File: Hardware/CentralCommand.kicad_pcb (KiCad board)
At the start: 4 copper layers, 65 parts, among them IC101 STM32F030C8, IC201 FT232RQ, P101 I2C, P102 GPIO1, P103 GPIO1, P104 USART, P105 SPI, P106 ADC, P201 USB_OTG, P202 POWER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

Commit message: layout almost done
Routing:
- net GND: track 89.1 -> 101.6 mm, vias 15 -> 21
- net /PWR: track 29.6 -> 41.4 mm, vias 6 -> 9
- net Net-(C107-Pad1): track 0.00 -> 7.28 mm, vias 0 -> 1

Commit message: relocated footprint labels
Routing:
- net /NRST: track 90.5 -> 92.0 mm
- net GND: track 101.6 -> 103.0 mm, vias 21 -> 22
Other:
- rule pad_to_mask_clearance: 0.2 -> 0.0635

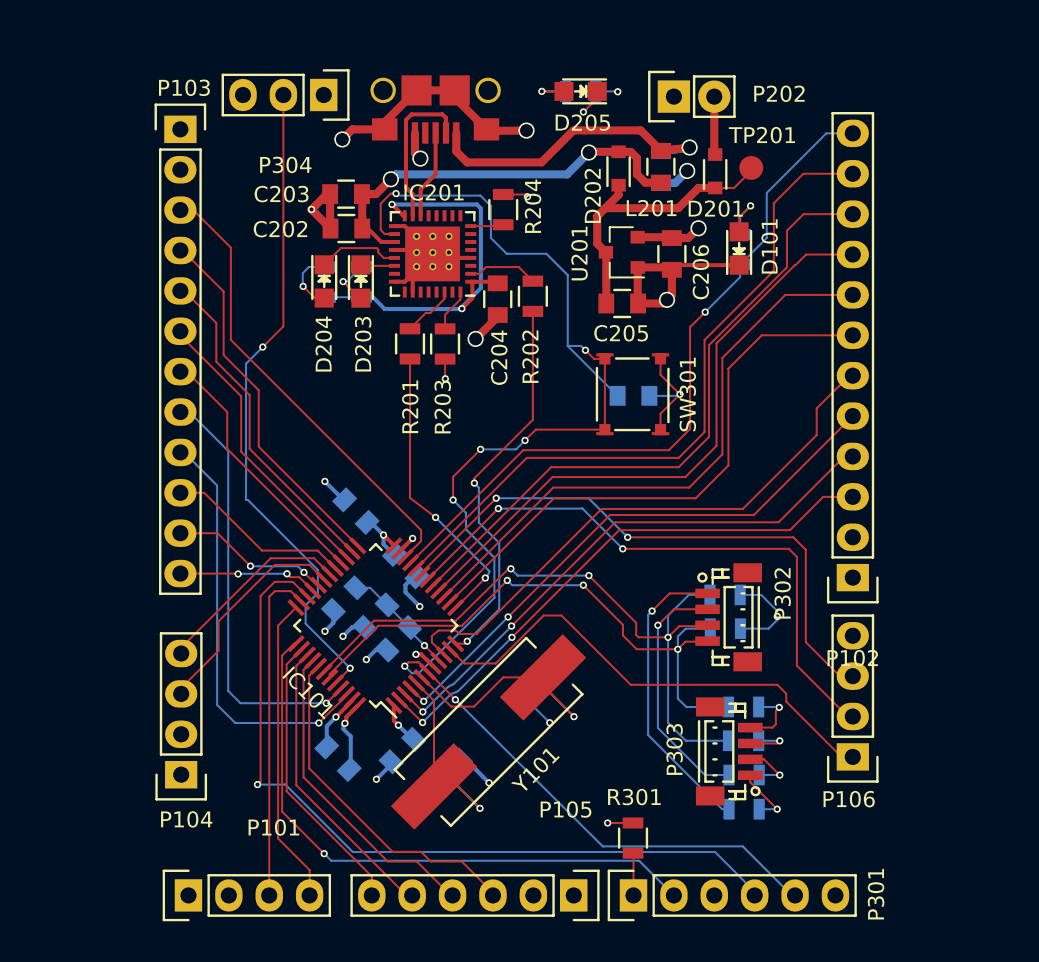
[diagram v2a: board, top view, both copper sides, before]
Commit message: labeled headers
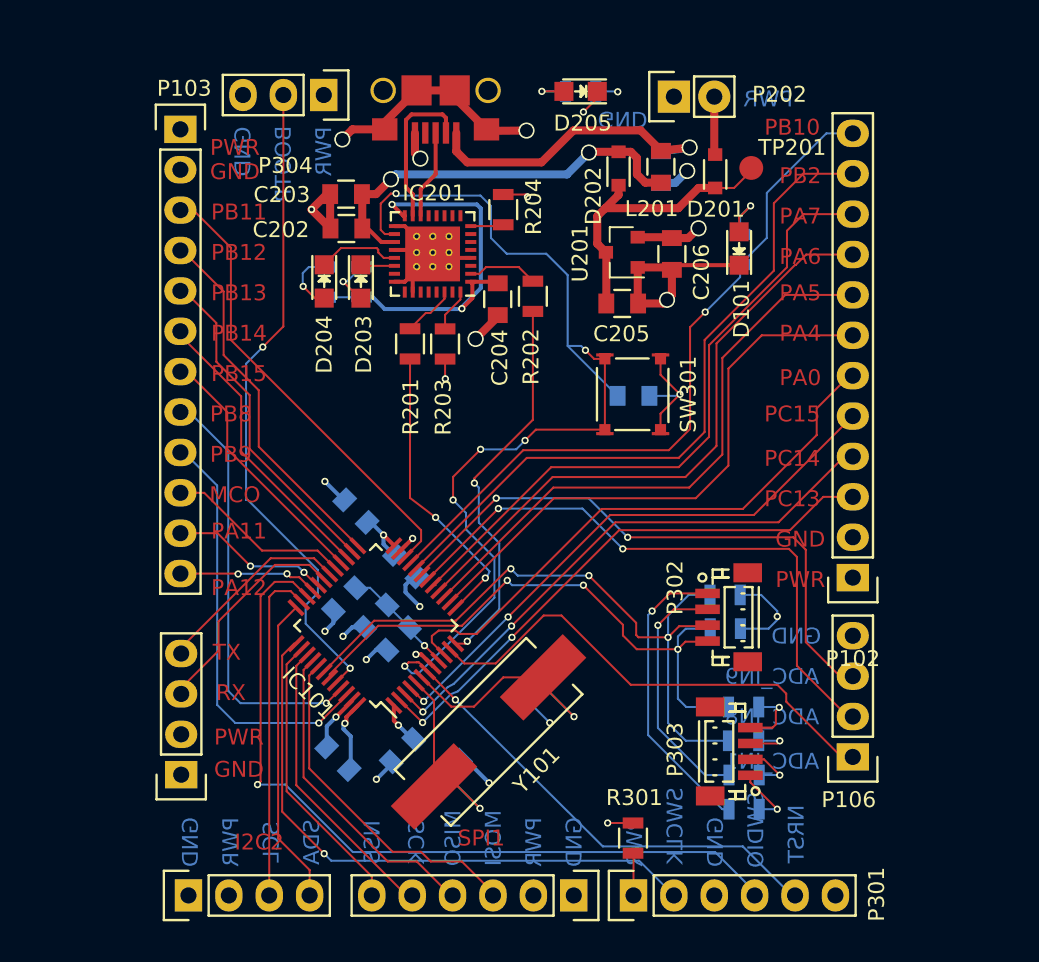
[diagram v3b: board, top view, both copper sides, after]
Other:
- board text added: "ADC_IN1"
- board text added: "ADC_IN8"
- board text added: "ADC_IN9"
- board text added: "BOOTP"
- board text added: "GND"
- board text added: "I2C2"
- board text added: "MCO"
- board text added: "MISO"
- board text added: "MOSI"
- board text added: "NRST"
- board text added: "NSS"
- board text added: "PA0"
- board text added: "PA11"
- board text added: "PA12"
- board text added: "PA4"
- board text added: "PA5"
- board text added: "PA6"
- board text added: "PA7"
- board text added: "PB10"
- board text added: "PB11"
- board text added: "PB12"
- board text added: "PB13"
- board text added: "PB14"
- board text added: "PB15"
- board text added: "PB2"
- board text added: "PB8"
- board text added: "PB9"
- board text added: "PC13"
- board text added: "PC14"
- board text added: "PC15"
- board text added: "PWR"
- board text added: "RX"
- board text added: "SCK"
- board text added: "SCL"
- board text added: "SDA"
- board text added: "SPI1"
- board text added: "SWCLK"
- board text added: "SWDIO"
- board text added: "TX"
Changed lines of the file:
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@@
     (links 170)
     (no_connects 0)
-    (area 102.583 63.83244 154.41038 122.4394)
+    (area 106.174999 62.9536 154.41038 122.4394)
     (thickness 1.6)
-    (drawings 0)
+    (drawings 54)
     (tracks 712)
     (zones 0)
@@
     (solder_mask_min_width 0.0635)
     (aux_axis_origin 0 0)
-    (visible_elements FFFEBD5F)
+    (visible_elements FFFEFF7F)
     (pcbplotparams
       (layerselection 0x00030_80000001)
@@
     (descr "Through hole pin header")
     (tags "pin header")
-    (fp_text reference P101 (at 4.23672 5.36956 180) (layer F.SilkS)
+    (fp_text reference P101 (at 4.23672 5.36956 180) (layer F.SilkS) hide
       (effects (font (size 1 1) (thickness 0.15)))
     )
@@
     (descr "Through hole pin header")
     (tags "pin header")
-    (fp_text reference P104 (at -0.32004 -2.84988 180) (layer F.SilkS)
+    (fp_text reference P104 (at -0.32004 -2.84988 180) (layer F.SilkS) hide
       (effects (font (size 1 1) (thickness 0.15)))
     )
@@
     (descr "Through hole pin header")
     (tags "pin header")
-    (fp_text reference P105 (at -5.36956 0.49276 360) (layer F.SilkS)
+    (fp_text reference P105 (at -5.36956 0.49276 360) (layer F.SilkS) hide
       (effects (font (size 1 1) (thickness 0.15)))
     )
@@
     (tags "connector jst sh")
     (attr smd)
-    (fp_text reference P302 (at -1.5 -3.5 270) (layer F.SilkS)
+    (fp_text reference P302 (at -1.85928 3.302 270) (layer F.SilkS)
       (effects (font (size 1 1) (thickness 0.15)))
     )
@@
     (tags "Mesurement Point Round SMD Pad 1.5mm")
     (attr virtual)
-    (fp_text reference TP201 (at 0.7366 -2.02692) (layer F.SilkS)
+    (fp_text reference TP201 (at 2.57556 -1.28524) (layer F.SilkS)
       (effects (font (size 1 1) (thickness 0.15)))
     )
@@
     (tags "LED 0805 SMD")
     (attr smd)
-    (fp_text reference D101 (at 0.12192 1.95834 90) (layer F.SilkS)
+    (fp_text reference D101 (at -3.81 0.15494 90) (layer F.SilkS)
       (effects (font (size 1 1) (thickness 0.15)))
     )
@@
       (net 2 GND) (zone_connect 2))
   )
+  (gr_text PWR (at 136.652 115.062 90) (layer B.Cu)
+    (effects (font (size 1 1) (thickness 0.15)) (justify mirror))
+  )
+  (gr_text SWCLK (at 139.192 114.046 90) (layer B.Cu)
+    (effects (font (size 1 1) (thickness 0.15)) (justify mirror))
+  )
+  (gr_text NRST (at 146.812 114.554 90) (layer B.Cu)
+    (effects (font (size 1 1) (thickness 0.15)) (justify mirror))
+  )
+  (gr_text SWDIO (at 144.272 114.3 90) (layer B.Cu)
+    (effects (font (size 1 1) (thickness 0.15)) (justify mirror))
+  )
+  (gr_text GND (at 141.732 115.062 90) (layer B.Cu)
+    (effects (font (size 1 1) (thickness 0.15)) (justify mirror))
+  )
+  (gr_text ADC_IN1 (at 145.288 109.982) (layer B.Cu)
+    (effects (font (size 1 1) (thickness 0.15)) (justify mirror))
+  )
+  (gr_text ADC_IN8 (at 145.288 107.188) (layer B.Cu)
+    (effects (font (size 1 1) (thickness 0.15)) (justify mirror))
+  )
+  (gr_text ADC_IN9 (at 145.288 104.648) (layer B.Cu)
+    (effects (font (size 1 1) (thickness 0.15)) (justify mirror))
+  )
+  (gr_text GND (at 146.812 102.108) (layer B.Cu)
+    (effects (font (size 1 1) (thickness 0.15)) (justify mirror))
+  )
+  (gr_text SPI1 (at 127 114.808) (layer F.Cu)
+    (effects (font (size 1 1) (thickness 0.15)))
+  )
+  (gr_text MOSI (at 127.762 114.808 90) (layer B.Cu)
+    (effects (font (size 1 1) (thickness 0.15)) (justify mirror))
+  )
+  (gr_text MISO (at 125.222 114.808 90) (layer B.Cu)
+    (effects (font (size 1 1) (thickness 0.15)) (justify mirror))
+  )
+  (gr_text NSS (at 120.142 115.062 90) (layer B.Cu)
+    (effects (font (size 1 1) (thickness 0.15)) (justify mirror))
+  )
+  (gr_text SCK (at 122.936 115.062 90) (layer B.Cu)
+    (effects (font (size 1 1) (thickness 0.15)) (justify mirror))
+  )
+  (gr_text GND (at 132.842 115.062 90) (layer B.Cu)
+    (effects (font (size 1 1) (thickness 0.15)) (justify mirror))
+  )
+  (gr_text PWR (at 130.302 115.062 90) (layer B.Cu)
+    (effects (font (size 1 1) (thickness 0.15)) (justify mirror))
+  )
+  (gr_text PWR (at 145.034 68.326) (layer B.Cu)
+    (effects (font (size 1 1) (thickness 0.15)) (justify mirror))
+  )
+  (gr_text GND (at 135.89 69.596 180) (layer B.Cu)
+    (effects (font (size 1 1) (thickness 0.15)) (justify mirror))
+  )
+  (gr_text BOOTP (at 114.554 72.39 90) (layer B.Cu)
+    (effects (font (size 1 1) (thickness 0.15)) (justify mirror))
+  )
+  (gr_text PWR (at 117.094 71.628 90) (layer B.Cu)
+    (effects (font (size 1 1) (thickness 0.15)) (justify mirror))
+  )
+  (gr_text GND (at 112.014 71.628 90) (layer B.Cu)
+    (effects (font (size 1 1) (thickness 0.15)) (justify mirror))
+  )
+  (gr_text I2C2 (at 113.03 115.062) (layer F.Cu)
+    (effects (font (size 1 1) (thickness 0.15)))
+  )
+  (gr_text SDA (at 116.332 115.062 90) (layer B.Cu)
+    (effects (font (size 1 1) (thickness 0.15)) (justify mirror))
+  )
+  (gr_text SCL (at 113.792 115.062 90) (layer B.Cu)
+    (effects (font (size 1 1) (thickness 0.15)) (justify mirror))
+  )
+  (gr_text PWR (at 111.252 115.062 90) (layer B.Cu)
+    (effects (font (size 1 1) (thickness 0.15)) (justify mirror))
+  )
+  (gr_text GND (at 108.712 115.062 90) (layer B.Cu)
+    (effects (font (size 1 1) (thickness 0.15)) (justify mirror))
+  )
+  (gr_text GND (at 111.76 110.49) (layer F.Cu)
+    (effects (font (size 1 1) (thickness 0.15)))
+  )
+  (gr_text PWR (at 111.76 108.458) (layer F.Cu)
+    (effects (font (size 1 1) (thickness 0.15)))
+  )
+  (gr_text RX (at 111.252 105.664) (layer F.Cu)
+    (effects (font (size 1 1) (thickness 0.15)))
+  )
+  (gr_text TX (at 110.998 103.124) (layer F.Cu)
+    (effects (font (size 1 1) (thickness 0.15)))
+  )
+  (gr_text PA12 (at 111.76 99.06) (layer F.Cu)
+    (effects (font (size 1 1) (thickness 0.15)))
+  )
+  (gr_text PA11 (at 111.76 95.504) (layer F.Cu)
+    (effects (font (size 1 1) (thickness 0.15)))
+  )
+  (gr_text MCO (at 111.506 93.218) (layer F.Cu)
+    (effects (font (size 1 1) (thickness 0.15)))
+  )
+  (gr_text PB9 (at 111.252 90.678) (layer F.Cu)
+    (effects (font (size 1 1) (thickness 0.15)))
+  )
+  (gr_text PB8 (at 111.252 88.138) (layer F.Cu)
+    (effects (font (size 1 1) (thickness 0.15)))
+  )
+  (gr_text PB15 (at 111.76 85.598) (layer F.Cu)
+    (effects (font (size 1 1) (thickness 0.15)))
+  )
+  (gr_text PB14 (at 111.76 83.058) (layer F.Cu)
+    (effects (font (size 1 1) (thickness 0.15)))
+  )
+  (gr_text PB13 (at 111.76 80.518) (layer F.Cu)
+    (effects (font (size 1 1) (thickness 0.15)))
+  )
+  (gr_text PB12 (at 111.76 77.978) (layer F.Cu)
+    (effects (font (size 1 1) (thickness 0.15)))
+  )
+  (gr_text PB11 (at 111.76 75.438) (layer F.Cu)
+    (effects (font (size 1 1) (thickness 0.15)))
+  )
+  (gr_text GND (at 111.506 72.898) (layer F.Cu)
+    (effects (font (size 1 1) (thickness 0.15)))
+  )
+  (gr_text PWR (at 111.506 71.374) (layer F.Cu)
+    (effects (font (size 1 1) (thickness 0.15)))
+  )
+  (gr_text PWR (at 147.066 98.552) (layer F.Cu)
+    (effects (font (size 1 1) (thickness 0.15)))
+  )
+  (gr_text GND (at 147.066 96.012) (layer F.Cu)
+    (effects (font (size 1 1) (thickness 0.15)))
+  )
+  (gr_text PC13 (at 146.558 93.472) (layer F.Cu)
+    (effects (font (size 1 1) (thickness 0.15)))
+  )
+  (gr_text PC14 (at 146.558 90.932) (layer F.Cu)
+    (effects (font (size 1 1) (thickness 0.15)))
+  )
+  (gr_text PC15 (at 146.558 88.138) (layer F.Cu)
+    (effects (font (size 1 1) (thickness 0.15)))
+  )
+  (gr_text PA0 (at 147.066 85.852) (layer F.Cu)
+    (effects (font (size 1 1) (thickness 0.15)))
+  )
+  (gr_text PA4 (at 147.066 83.058) (layer F.Cu)
+    (effects (font (size 1 1) (thickness 0.15)))
+  )
+  (gr_text PA5 (at 147.066 80.518) (layer F.Cu)
+    (effects (font (size 1 1) (thickness 0.15)))
+  )
+  (gr_text PB10 (at 146.558 70.104) (layer F.Cu)
+    (effects (font (size 1 1) (thickness 0.15)))
+  )
+  (gr_text PB2 (at 147.066 73.152) (layer F.Cu)
+    (effects (font (size 1 1) (thickness 0.15)))
+  )
+  (gr_text PA7 (at 147.066 75.692) (layer F.Cu)
+    (effects (font (size 1 1) (thickness 0.15)))
+  )
+  (gr_text PA6 (at 147.066 78.232) (layer F.Cu)
+    (effects (font (size 1 1) (thickness 0.15)))
+  )
   (segment (start 130.885862 104.699138) (end 130.885862 105.221702) (width 0.127) (layer F.Cu) (net 1))

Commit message: adjusted a few more labels, added mounting holes, generated gerbers
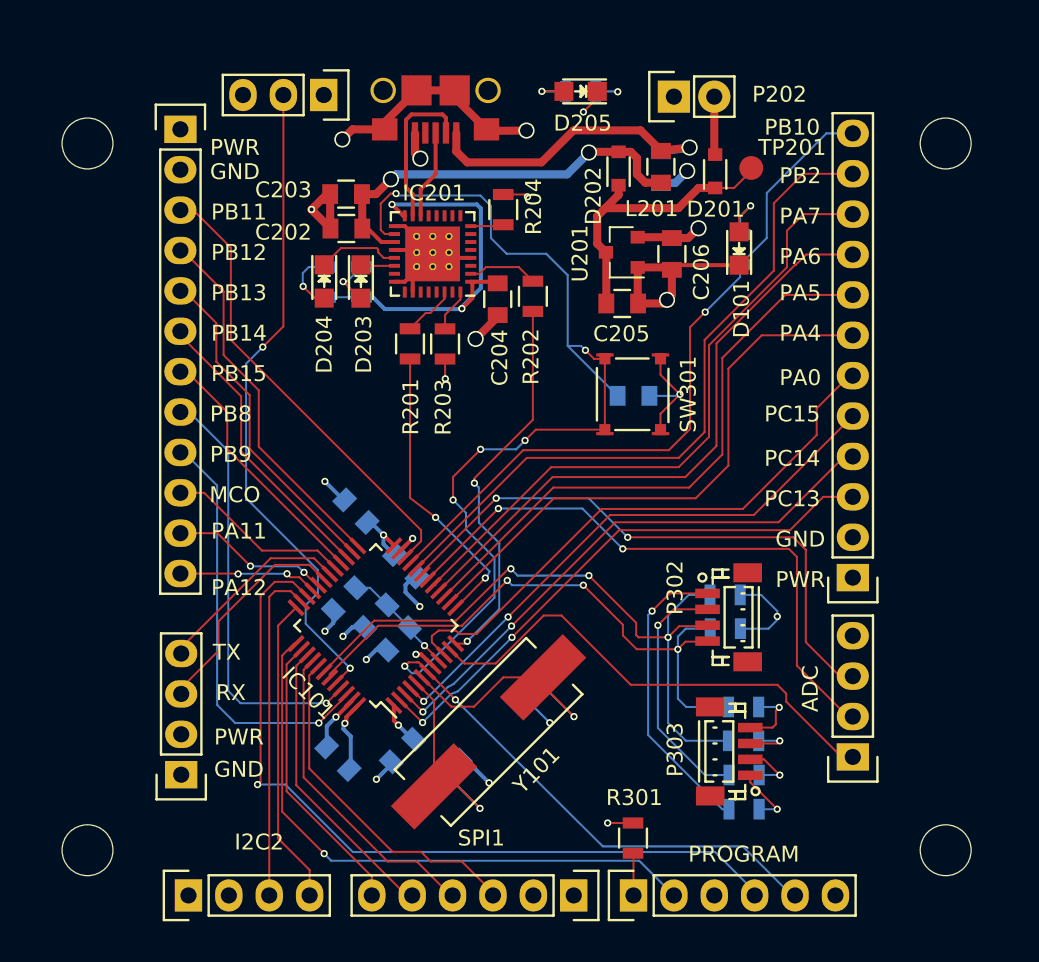
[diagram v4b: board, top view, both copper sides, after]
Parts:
- added REF**: MountingHole_3.2mm_M3, Mounting_Holes:MountingHole_3.2mm_M3, F.Cu at (156.2, 71.1)
- added REF**: MountingHole_3.2mm_M3, Mounting_Holes:MountingHole_3.2mm_M3, F.Cu at (156.2, 115.6)
- added REF**: MountingHole_3.2mm_M3, Mounting_Holes:MountingHole_3.2mm_M3, F.Cu at (102.2, 115.6)
- added REF**: MountingHole_3.2mm_M3, Mounting_Holes:MountingHole_3.2mm_M3, F.Cu at (102.2, 71.1)
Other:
- board text added: "ADC"
- board text added: "AUX POWER"
- board text added: "Central Command Alan Ford"
- board text added: "PROGRAM"

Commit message: bring everything up-to-date
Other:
- board outline added: 61.2 x 54.5 mm
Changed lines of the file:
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@@
     (area 92.750857 63.83244 165.694143 122.4394)
     (thickness 1.6)
-    (drawings 58)
+    (drawings 62)
     (tracks 712)
     (zones 0)
@@
   (layers
     (0 F.Cu signal)
-    (1 GND signal)
-    (2 PWR signal)
+    (1 GND signal hide)
+    (2 PWR signal hide)
     (31 B.Cu signal)
     (32 B.Adhes user)
@@
     (34 B.Paste user)
     (35 F.Paste user)
-    (36 B.SilkS user)
+    (36 B.SilkS user hide)
     (37 F.SilkS user)
     (38 B.Mask user)
@@
     (tags "resistor 0805")
     (attr smd)
-    (fp_text reference R207 (at 0.1016 2.22504) (layer B.SilkS)
+    (fp_text reference R207 (at -0.6604 2.2606) (layer B.SilkS)
       (effects (font (size 1 1) (thickness 0.15)) (justify mirror))
     )
@@
     (tags "resistor 0805")
     (attr smd)
-    (fp_text reference R302 (at -3.90144 0.00508) (layer B.SilkS)
+    (fp_text reference R302 (at -3.79984 -1.15316) (layer B.SilkS)
       (effects (font (size 1 1) (thickness 0.15)) (justify mirror))
     )
@@
     (tags "resistor 0805")
     (attr smd)
-    (fp_text reference R303 (at -3.82524 0.0508) (layer B.SilkS)
+    (fp_text reference R303 (at -3.79984 -1.4986) (layer B.SilkS)
       (effects (font (size 1 1) (thickness 0.15)) (justify mirror))
     )
@@
     (tags "resistor 0805")
     (attr smd)
-    (fp_text reference R304 (at -3.74396 0.05588) (layer B.SilkS)
+    (fp_text reference R304 (at -3.83032 -1.87452) (layer B.SilkS)
       (effects (font (size 1 1) (thickness 0.15)) (justify mirror))
     )
@@
     (tags "resistor 0805")
     (attr smd)
-    (fp_text reference R305 (at -3.77444 0.05588) (layer B.SilkS)
+    (fp_text reference R305 (at -3.83032 -2.49936) (layer B.SilkS)
       (effects (font (size 1 1) (thickness 0.15)) (justify mirror))
     )
@@
     (pad 1 np_thru_hole circle (at 0 0) (size 3.2 3.2) (drill 3.2) (layers *.Cu *.Mask))
   )
+  (gr_line (start 160.02 66.04) (end 98.806 66.04) (angle 90) (layer Edge.Cuts) (width 0.15))
+  (gr_line (start 160.02 120.523) (end 160.02 66.04) (angle 90) (layer Edge.Cuts) (width 0.15))
+  (gr_line (start 98.806 120.523) (end 160.02 120.523) (angle 90) (layer Edge.Cuts) (width 0.15))
+  (gr_line (start 98.806 66.04) (end 98.806 120.523) (angle 90) (layer Edge.Cuts) (width 0.15))
   (gr_text "AUX\nPOWER" (at 143.637 70.993) (layer B.SilkS)
     (effects (font (size 1 1) (thickness 0.15)) (justify mirror))
@@
     (effects (font (size 1 1) (thickness 0.15)) (justify mirror))
   )
-  (gr_text NRST (at 146.812 114.554 90) (layer B.SilkS)
+  (gr_text NRST (at 148.59 115.57 45) (layer B.SilkS)
     (effects (font (size 1 1) (thickness 0.15)) (justify mirror))
   )
-  (gr_text SWDIO (at 144.272 114.3 90) (layer B.SilkS)
+  (gr_text SWDIO (at 146.304 114.808 45) (layer B.SilkS)
     (effects (font (size 1 1) (thickness 0.15)) (justify mirror))
   )
-  (gr_text GND (at 141.732 115.062 90) (layer B.SilkS)
+  (gr_text GND (at 141.224 115.062 90) (layer B.SilkS)
     (effects (font (size 1 1) (thickness 0.15)) (justify mirror))
   )
-  (gr_text ADC_IN1 (at 145.288 109.982) (layer B.SilkS)
+  (gr_text ADC_IN1 (at 155.194 109.728) (layer B.SilkS)
     (effects (font (size 1 1) (thickness 0.15)) (justify mirror))
   )
-  (gr_text ADC_IN8 (at 145.288 107.188) (layer B.SilkS)
+  (gr_text ADC_IN8 (at 155.194 107.188) (layer B.SilkS)
     (effects (font (size 1 1) (thickness 0.15)) (justify mirror))
   )
-  (gr_text ADC_IN9 (at 145.288 104.648) (layer B.SilkS)
+  (gr_text ADC_IN9 (at 155.194 104.648) (layer B.SilkS)
     (effects (font (size 1 1) (thickness 0.15)) (justify mirror))
   )
-  (gr_text GND (at 146.812 102.108) (layer B.SilkS)
+  (gr_text GND (at 153.67 102.108) (layer B.SilkS)
     (effects (font (size 1 1) (thickness 0.15)) (justify mirror))
   )
-  (gr_text SPI1 (at 127 114.808) (layer F.SilkS)
+  (gr_text SPI1 (at 126.238 115.824) (layer F.SilkS)
     (effects (font (size 1 1) (thickness 0.15)))
   )
@@
     (effects (font (size 1 1) (thickness 0.15)) (justify mirror))
   )
-  (gr_text GND (at 135.89 69.596 180) (layer B.SilkS)
+  (gr_text GND (at 136.398 69.85 180) (layer B.SilkS)
     (effects (font (size 1 1) (thickness 0.15)) (justify mirror))
   )
@@
     (effects (font (size 1 1) (thickness 0.15)) (justify mirror))
   )
-  (gr_text I2C2 (at 113.03 115.062) (layer F.SilkS)
+  (gr_text I2C2 (at 113.284 115.824) (layer F.SilkS)
     (effects (font (size 1 1) (thickness 0.15)))
   )
@@
     (polygon
       (pts
-        (xy 160.02 120.396) (xy 98.7298 120.51284) (xy 98.755094 66.039342) (xy 160.528 66.04)
+        (xy 160.02 120.523) (xy 98.806 120.523) (xy 98.806 66.04) (xy 160.02 66.04)
       )
     )
@@
     (polygon
       (pts
-        (xy 159.9184 120.396) (xy 98.7044 120.5484) (xy 98.806 65.9892) (xy 160.6296 65.9892)
+        (xy 160.02 120.523) (xy 98.806 120.523) (xy 98.806 66.04) (xy 160.02 66.04)
       )
     )
